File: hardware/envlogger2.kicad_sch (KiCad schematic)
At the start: 6 parts, among them U1 STM32L432KCUx

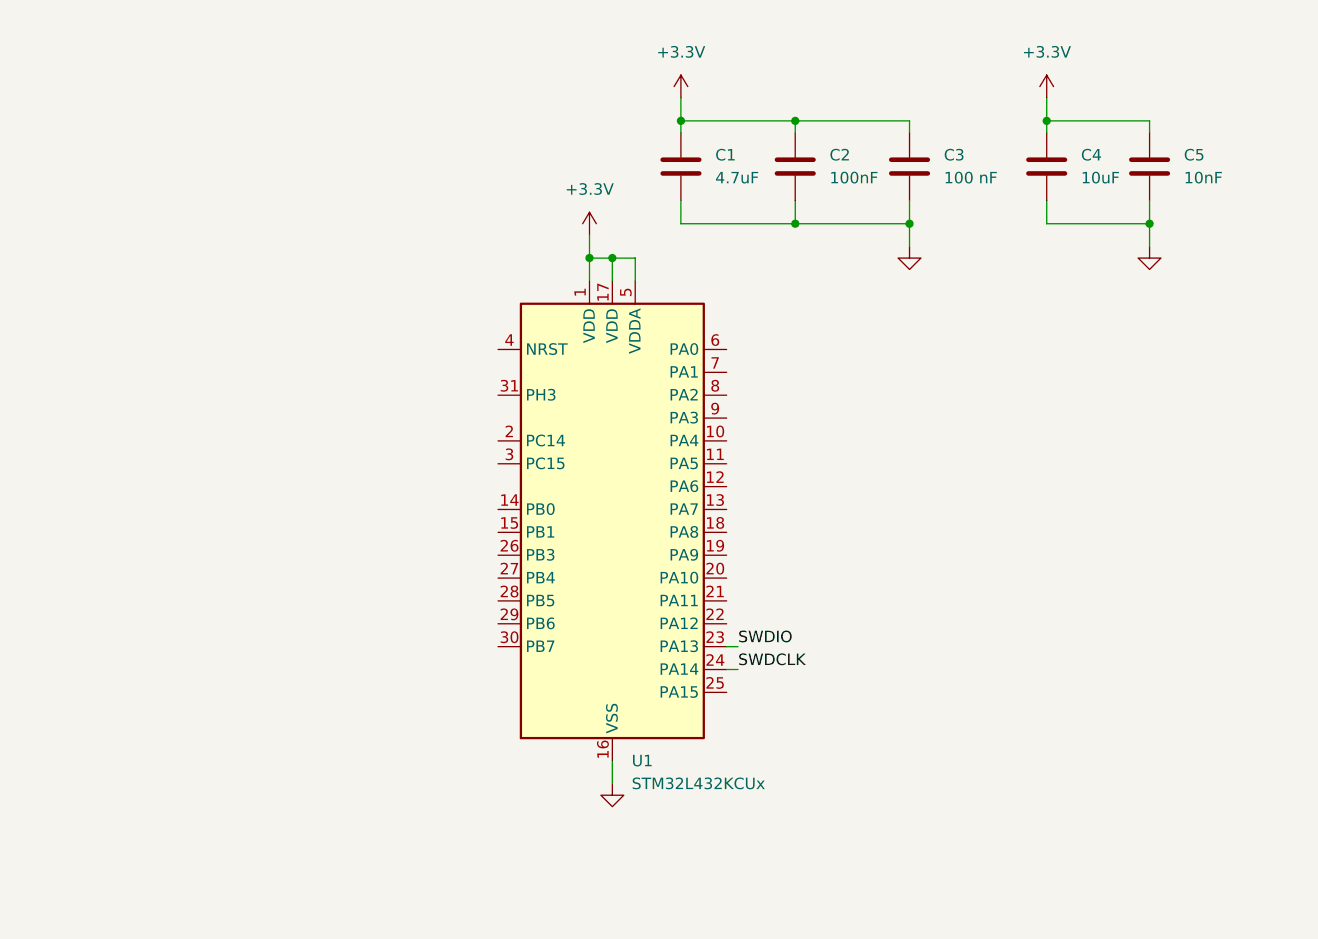
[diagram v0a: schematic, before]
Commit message: Added MCU wiring to schematic
Decoupling, crystal, connectors, etc.
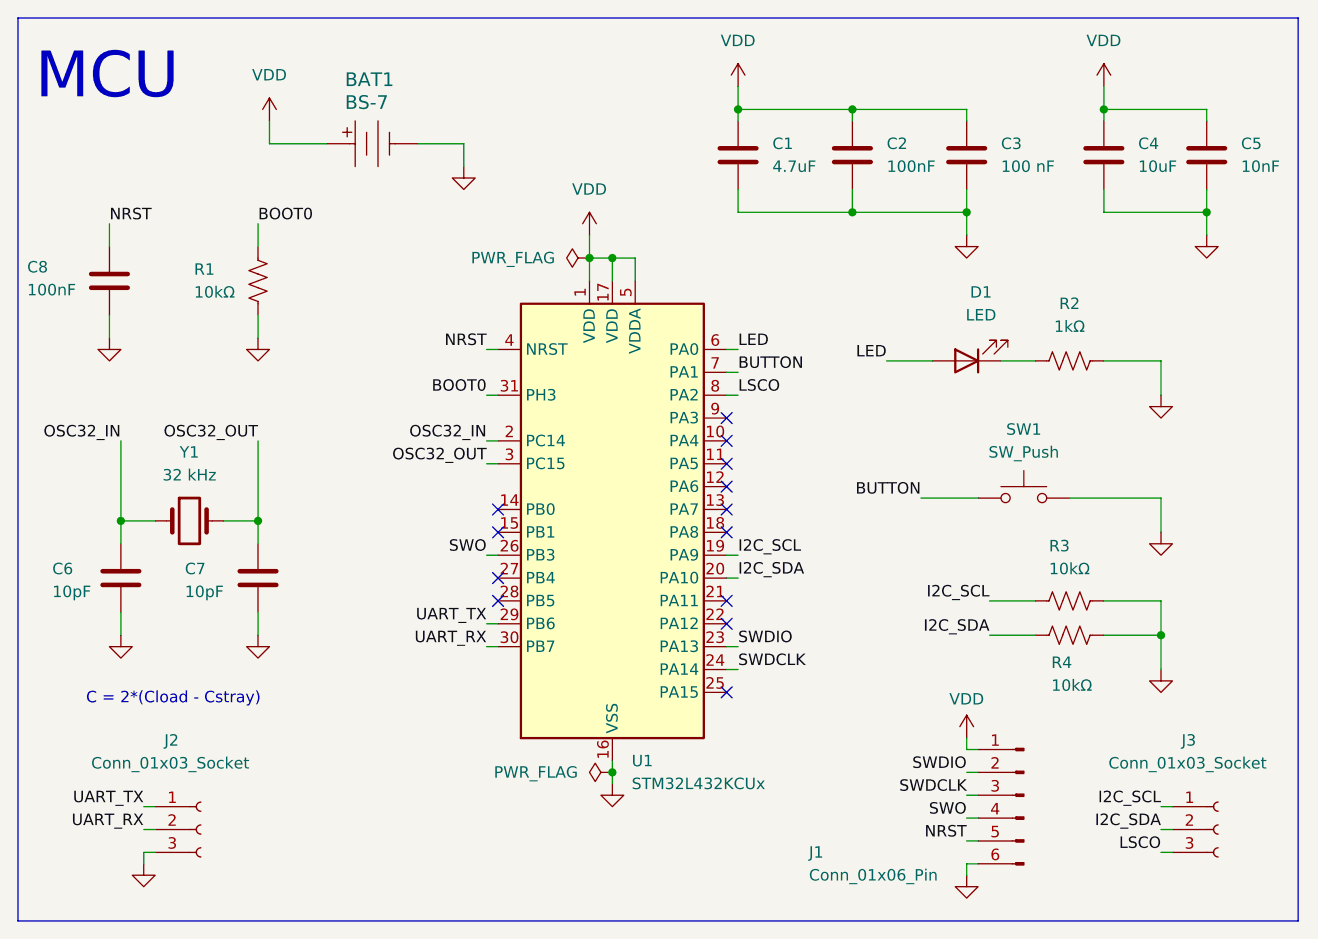
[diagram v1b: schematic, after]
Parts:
- added BAT1: BS-7, digikey-footprints:Battery_Holder_Coin_2032_BS-7, symbol dk_Battery-Holders-Clips-Contacts:BS-7
- added C6, C7: 10pF, symbol Device:C
- added C8: 100nF, symbol Device:C
- added D1: LED, symbol Device:LED
- added J1: Conn_01x06_Pin, symbol Connector:Conn_01x06_Pin
- added J2, J3: Conn_01x03_Socket, symbol Connector:Conn_01x03_Socket
- added R1, R3, R4: 10kΩ, symbol Device:R_US
- added R2: 1kΩ, symbol Device:R_US
- added SW1: SW_Push, symbol Switch:SW_Push
- added Y1: 32 kHz, symbol Device:Crystal
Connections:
- net GND: now also BAT1.Neg, C6.1, C7.2, C8.2, J1.6 (Pin_6), J2.3 (Pin_3), R1.1, R2.2, R3.1, R4.1, SW1.2
- net SWDCLK: now also J1.3 (Pin_3)
- net SWDIO: now also J1.2 (Pin_2)
- net I2C_SCL: now reaches U1.19 (PA9)
- net I2C_SCL: now also J3.1 (Pin_1), R3.2
- net OSC32_IN: now reaches U1.2 (PC14)
- net OSC32_IN: now also C6.2, Y1.1
- net I2C_SDA: now reaches U1.20 (PA10)
- net I2C_SDA: now also J3.2 (Pin_2), R4.2
- net SWO: now reaches U1.26 (PB3)
- net SWO: now also J1.4 (Pin_4)
- net UART_TX: now reaches U1.29 (PB6)
- net UART_TX: now also J2.1 (Pin_1)
- net OSC32_OUT: now reaches U1.3 (PC15)
- net OSC32_OUT: now also C7.1, Y1.2
- net UART_RX: now reaches U1.30 (PB7)
- net UART_RX: now also J2.2 (Pin_2)
- net BOOT0: now reaches U1.31 (PH3)
- net BOOT0: now also R1.2
- net NRST: now reaches U1.4 (NRST)
- net NRST: now also C8.1, J1.5 (Pin_5)
- net LED: now reaches U1.6 (PA0)
- net LED: now also D1.2 (A)
- net BUTTON: now reaches U1.7 (PA1)
- net BUTTON: now also SW1.1
- net LSCO: now reaches U1.8 (PA2)
- net LSCO: now also J3.3 (Pin_3)
- net +3.3V renamed VDD
- net VDD: now also BAT1.Pos, J1.1 (Pin_1)
- new net: D1.1 (K), R2.1
- no-connect marks 0 -> 13
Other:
- note added: "C = 2*(Cload - Cstray)"
- note added: "MCU"
- moved on the sheet: C1, C2, C3, C4, C5
